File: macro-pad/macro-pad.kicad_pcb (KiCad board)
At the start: 2 copper layers, 100 x 100 mm, 83 parts, among them J1 USB_C_Receptacle_USB2.0, J2 Conn_01x04, J8 Conn_01x06, Q1 2N7002, SW1 Rotary_Encoder_Switch, U1 USBLC6-2SC6, U2 ATmega32U4-AU, Y1 Crystal_GND24

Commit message: add case plates generation
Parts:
- removed H1: MountingHole, MountingHole:MountingHole_3.2mm_M3
- H2, H3, H4, H5: footprint MountingHole:MountingHole_3.2mm_M3 -> keeb-conn:MountingHole_3.2mm_M3
- MX1, MX10, MX12, MX13, MX14, MX15, MX16, MX18, MX2, MX3, MX4, MX7, MX8, MX9: footprint ai03-MX_only:MXOnly-1U -> ai03-MX_only:MXOnly-1U-Hotswap-Antishear-Led-SMD
- MX20, MX22, MX5: footprint ai03-MX_only:MXOnly-2U -> ai03-MX_only:MXOnly-2U-Hotswap-Antishear-Led-SMD

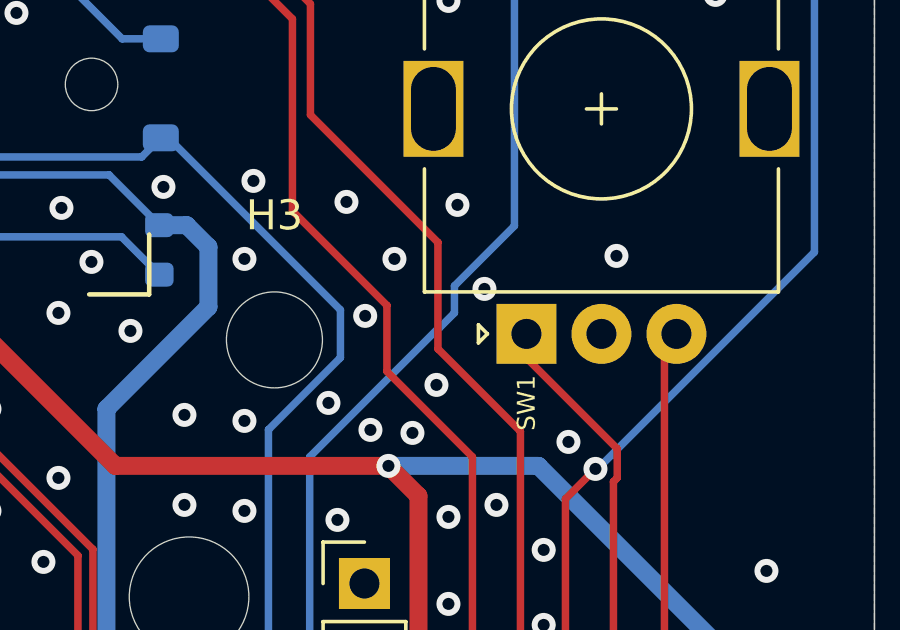
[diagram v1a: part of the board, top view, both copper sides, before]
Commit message: update lib for correct cad generation
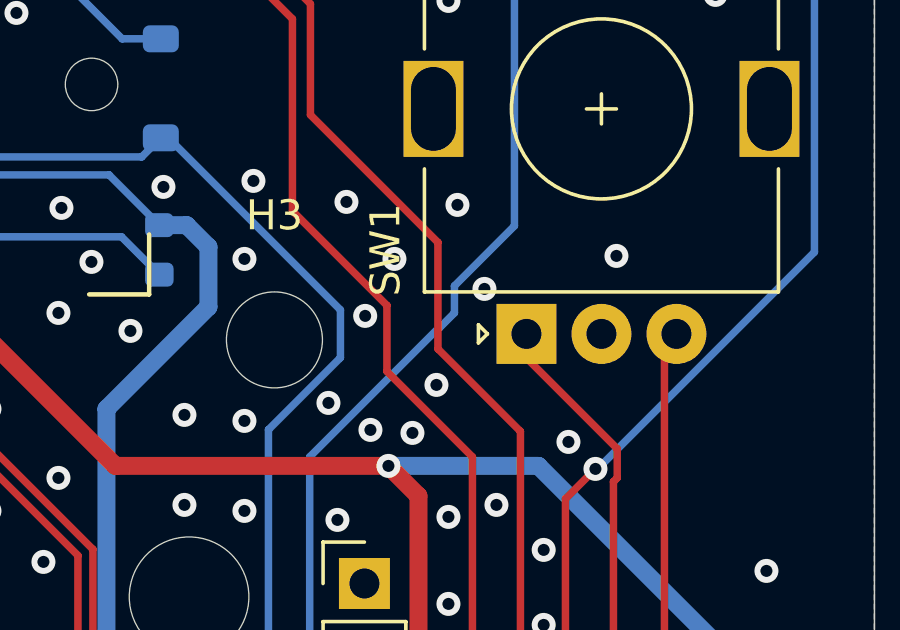
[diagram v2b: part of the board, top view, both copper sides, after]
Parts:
- SW1: footprint Rotary_Encoder:RotaryEncoder_Alps_EC11E-Switch_Vertical_H20mm -> keeb-conn:RotaryEncoder_Alps_EC11E-Switch_Vertical_H20mm
